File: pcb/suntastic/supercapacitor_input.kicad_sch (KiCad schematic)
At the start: 4 parts, among them J3 Supercap IN

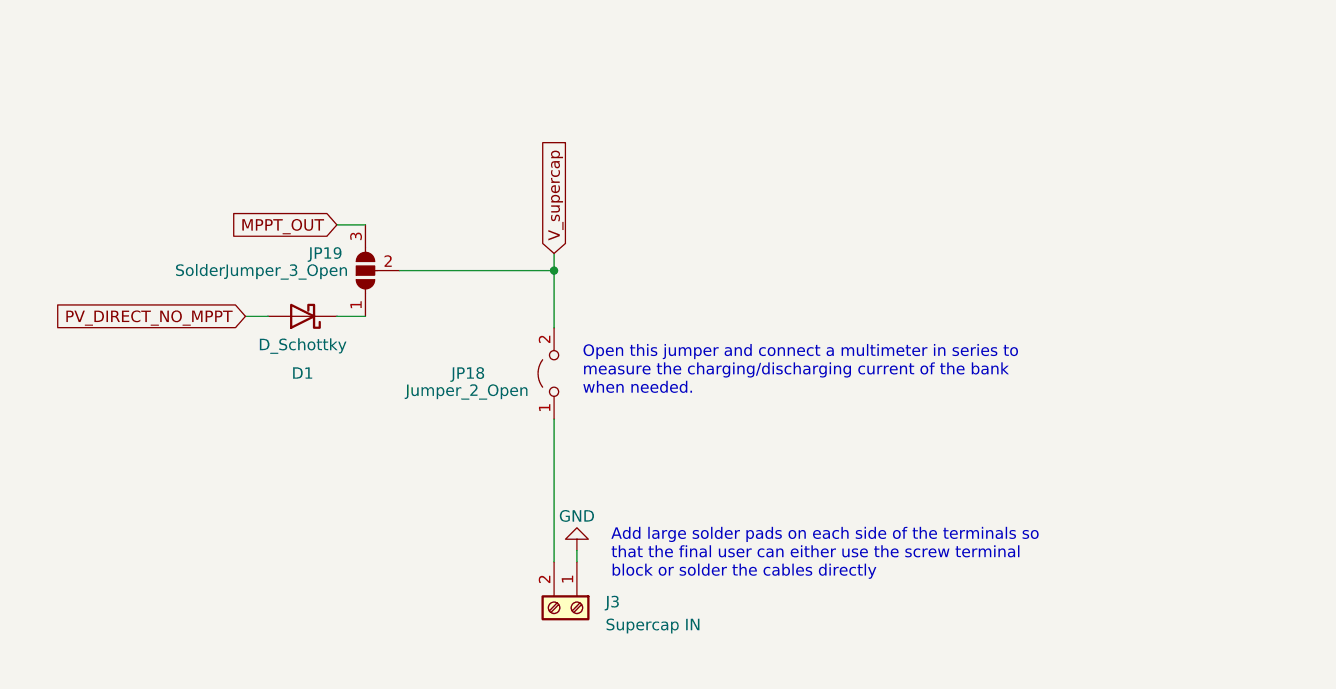
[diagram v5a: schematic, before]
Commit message: Update footprints
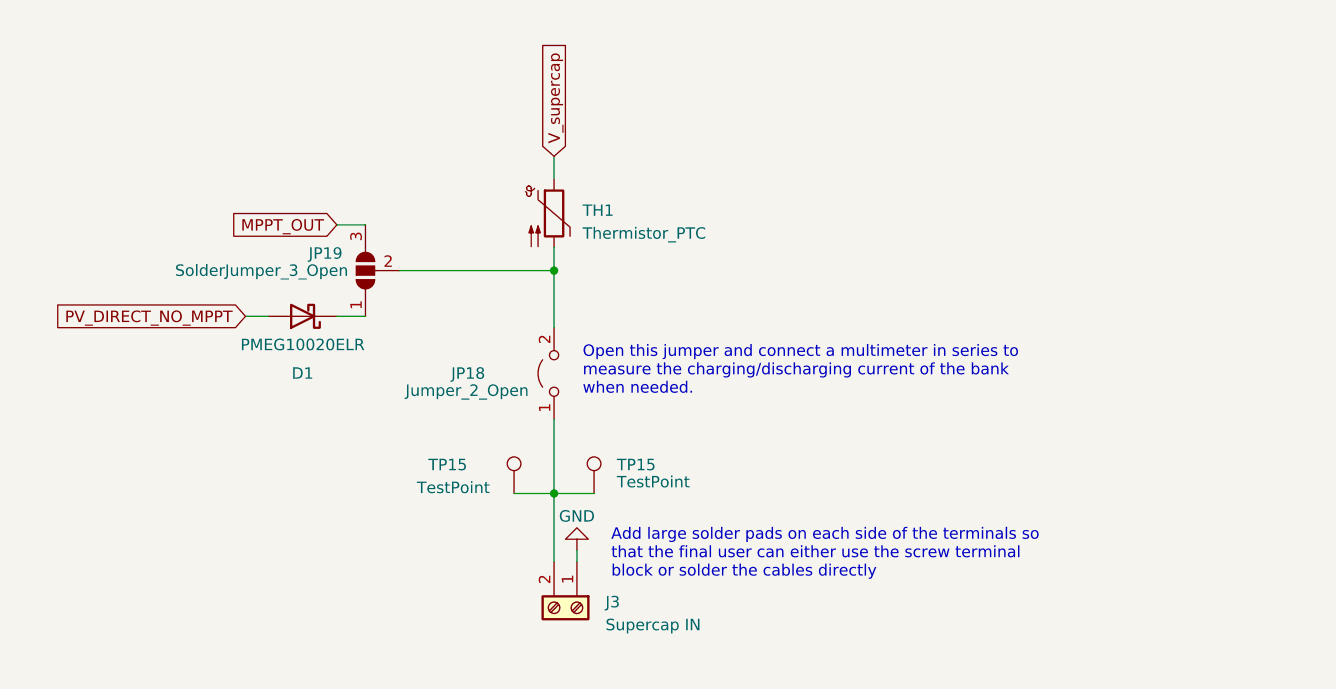
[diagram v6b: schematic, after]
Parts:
- added TH1: Thermistor_PTC, Resistor_SMD:R_0603_1608Metric_Pad0.98x0.95mm_HandSolder, symbol Device:Thermistor_PTC
- added TP15 (x2): TestPoint, TestPoint:TestPoint_THTPad_4.0x4.0mm_Drill2.0mm, symbol Connector:TestPoint
- D1: value D_Schottky -> PMEG10020ELR; footprint (none) -> Diode_SMD:D_SOD-123F
- JP19: footprint (none) -> Jumper:SolderJumper-3_P1.3mm_Open_RoundedPad1.0x1.5mm_NumberLabels
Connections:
- net V_supercap: now also TH1.1; no longer JP18.2 (B), JP19.2 (C)
- net at J3.2 (Pin_2), JP18.1 (A): now also TP15.1, TP15.1
- new net: JP18.2 (B), JP19.2 (C), TH1.2
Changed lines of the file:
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@@
     (comment 4 "The voltage tolerated by the supercapacitor bank should be AT LEAST 5.4V.")
   )
+  (junction (at 150.495 83.185) (diameter 0) (color 0 0 0 0)
+  )
   (junction (at 150.495 58.42) (diameter 0) (color 0 0 0 0)
   )
-  (wire (pts (xy 150.495 74.93) (xy 150.495 90.805))
+  (wire (pts (xy 150.495 83.185) (xy 150.495 90.805))
+    (stroke (width 0) (type default))
+  )
+  (wire (pts (xy 150.495 74.93) (xy 150.495 83.185))
     (stroke (width 0) (type default))
   )
@@
     (stroke (width 0) (type default))
   )
-  (wire (pts (xy 150.495 56.515) (xy 150.495 58.42))
-    (stroke (width 0) (type default))
-  )
   (wire (pts (xy 150.495 58.42) (xy 150.495 64.77))
     (stroke (width 0) (type default))
   )
   (wire (pts (xy 133.35 58.42) (xy 150.495 58.42))
+    (stroke (width 0) (type default))
+  )
+  (wire (pts (xy 150.495 45.72) (xy 150.495 48.26))
+    (stroke (width 0) (type default))
+  )
+  (wire (pts (xy 150.495 55.88) (xy 150.495 58.42))
+    (stroke (width 0) (type default))
+  )
+  (wire (pts (xy 146.05 83.185) (xy 150.495 83.185))
+    (stroke (width 0) (type default))
+  )
+  (wire (pts (xy 150.495 83.185) (xy 154.94 83.185))
     (stroke (width 0) (type default))
   )
@@
     )
   )
-  (global_label "V_supercap" (shape input) (at 150.495 56.515 90) (fields_autoplaced)
+  (global_label "V_supercap" (shape input) (at 150.495 45.72 90) (fields_autoplaced)
     (effects (font (size 1.27 1.27)) (justify left))
-    (property "Intersheetrefs" "${INTERSHEET_REFS}" (at 150.495 42.9655 90)
+    (property "Intersheetrefs" "${INTERSHEET_REFS}" (at 150.495 32.1705 90)
       (effects (font (size 1.27 1.27)) (justify left) hide)
     )
@@
         (path "/4d5a6178-89d6-4824-ac30-5dee40aabff2/70576ca8-d50a-4f6d-b4d0-36474c2d5281"
           (reference "JP18") (unit 1)
+        )
+      )
+    )
+  )
+  (symbol (lib_id "Connector:TestPoint") (at 154.94 83.185 0) (unit 1)
+    (in_bom yes) (on_board yes) (dnp no)
+    (property "Reference" "TP15" (at 157.48 80.01 0)
+      (effects (font (size 1.27 1.27)) (justify left))
+    )
+    (property "Value" "TestPoint" (at 157.48 81.915 0)
+      (effects (font (size 1.27 1.27)) (justify left))
+    )
+    (property "Footprint" "TestPoint:TestPoint_THTPad_4.0x4.0mm_Drill2.0mm" (at 160.02 83.185 0)
+      (effects (font (size 1.27 1.27)) hide)
+    )
+    (property "Datasheet" "~" (at 160.02 83.185 0)
+      (effects (font (size 1.27 1.27)) hide)
+    )
+    (pin "1")
+    (instances
+      (project "suntastic"
+        (path "/4d5a6178-89d6-4824-ac30-5dee40aabff2/fadcfaa3-5ba9-44dc-a564-21a258e74f25"
+          (reference "TP15") (unit 1)
+        )
+        (path "/4d5a6178-89d6-4824-ac30-5dee40aabff2/70576ca8-d50a-4f6d-b4d0-36474c2d5281"
+          (reference "TP20") (unit 1)
         )
       )
@@
       (effects (font (size 1.27 1.27)))
     )
-    (property "Value" "D_Schottky" (at 122.555 66.675 0)
+    (property "Value" "PMEG10020ELR" (at 122.555 66.675 0)
       (effects (font (size 1.27 1.27)))
     )
-    (property "Footprint" "" (at 122.555 63.5 0)
-      (effects (font (size 1.27 1.27)) hide)
-    )
-    (property "Datasheet" "~" (at 122.555 63.5 0)
+    (property "Footprint" "Diode_SMD:D_SOD-123F" (at 122.555 63.5 0)
+      (effects (font (size 1.27 1.27)) hide)
+    )
+    (property "Datasheet" "https://assets.nexperia.com/documents/data-sheet/PMEG10020ELR.pdf" (at 122.555 63.5 0)
       (effects (font (size 1.27 1.27)) hide)
     )
@@
     )
   )
+  (symbol (lib_id "Device:Thermistor_PTC") (at 150.495 52.07 0) (unit 1)
+    (in_bom yes) (on_board yes) (dnp no) (fields_autoplaced)
+    (property "Reference" "TH1" (at 153.67 51.7525 0)
+      (effects (font (size 1.27 1.27)) (justify left))
+    )
+    (property "Value" "Thermistor_PTC" (at 153.67 54.2925 0)
+      (effects (font (size 1.27 1.27)) (justify left))
+    )
+    (property "Footprint" "Resistor_SMD:R_0603_1608Metric_Pad0.98x0.95mm_HandSolder" (at 151.765 57.15 0)
+      (effects (font (size 1.27 1.27)) (justify left) hide)
+    )
+    (property "Datasheet" "~" (at 150.495 52.07 0)
+      (effects (font (size 1.27 1.27)) hide)
+    )
+    (pin "1")
+    (pin "2")
+    (instances
+      (project "suntastic"
+        (path "/4d5a6178-89d6-4824-ac30-5dee40aabff2/70576ca8-d50a-4f6d-b4d0-36474c2d5281"
+          (reference "TH1") (unit 1)
+        )
+      )
+    )
+  )
+  (symbol (lib_id "Connector:TestPoint") (at 146.05 83.185 0) (unit 1)
+    (in_bom yes) (on_board yes) (dnp no)
+    (property "Reference" "TP15" (at 136.525 80.01 0)
+      (effects (font (size 1.27 1.27)) (justify left))
+    )
+    (property "Value" "TestPoint" (at 135.255 82.55 0)
+      (effects (font (size 1.27 1.27)) (justify left))
+    )
+    (property "Footprint" "TestPoint:TestPoint_THTPad_4.0x4.0mm_Drill2.0mm" (at 151.13 83.185 0)
+      (effects (font (size 1.27 1.27)) hide)
+    )
+    (property "Datasheet" "~" (at 151.13 83.185 0)
+      (effects (font (size 1.27 1.27)) hide)
+    )
+    (pin "1")
+    (instances
+      (project "suntastic"
+        (path "/4d5a6178-89d6-4824-ac30-5dee40aabff2/fadcfaa3-5ba9-44dc-a564-21a258e74f25"
+          (reference "TP15") (unit 1)
+        )
+        (path "/4d5a6178-89d6-4824-ac30-5dee40aabff2/70576ca8-d50a-4f6d-b4d0-36474c2d5281"
+          (reference "TP19") (unit 1)
+        )
+      )
+    )
+  )
   (symbol (lib_id "Jumper:SolderJumper_3_Open") (at 129.54 58.42 90) (unit 1)
     (in_bom yes) (on_board yes) (dnp no)
@@
       (effects (font (size 1.27 1.27)) (justify left))
     )
-    (property "Footprint" "" (at 129.54 58.42 0)
-      (effects (font (size 1.27 1.27)) hide)
-    )
+    (property "Footprint" "Jumper:SolderJumper-3_P1.3mm_Open_RoundedPad1.0x1.5mm_NumberLabels" (at 129.54 58.42 0)
+      (effects (font (size 1.27 1.27)) hide)
+    )

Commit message: Update more footprints and start with PCB
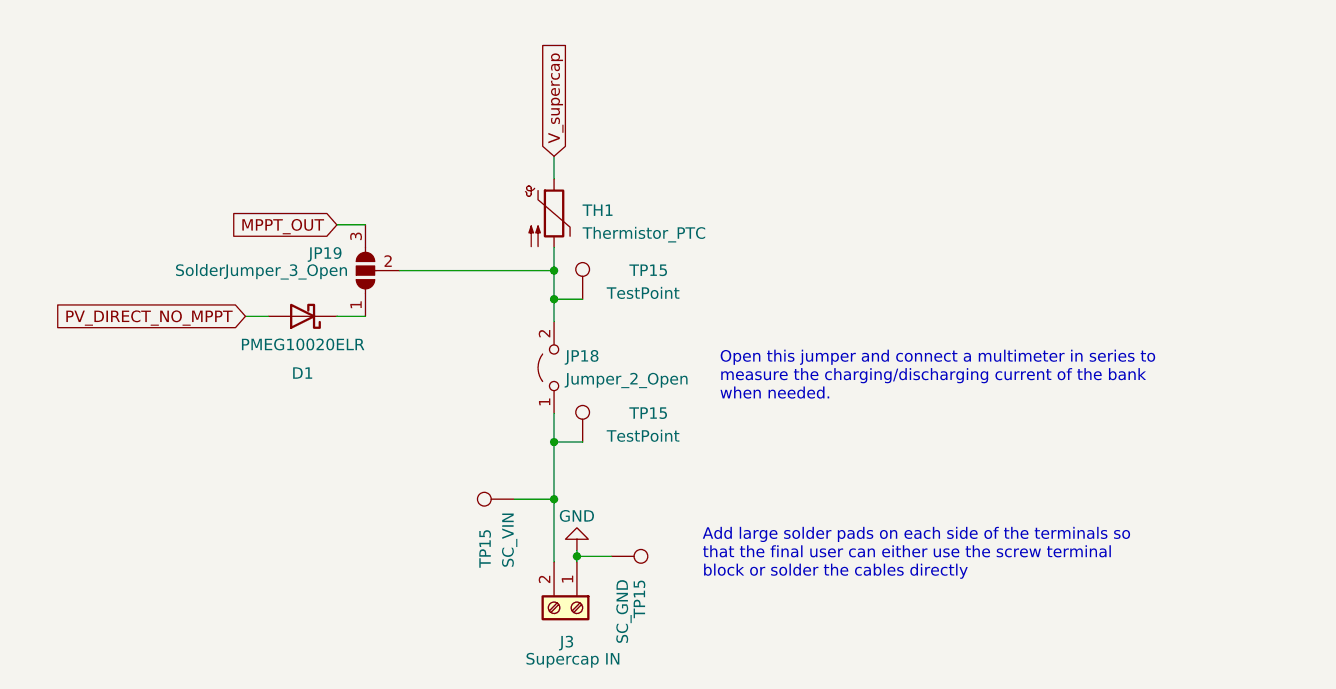
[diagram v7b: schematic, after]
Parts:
- added TP15 (x2): TestPoint, TestPoint:TestPoint_Bridge_Pitch5.08mm_Drill1.3mm, symbol Connector:TestPoint
- JP18: footprint (none) -> Jumper:SolderJumper-2_P1.3mm_Open_RoundedPad1.0x1.5mm
- TP15: value TestPoint -> SC_GND
- TP15: value TestPoint -> SC_VIN
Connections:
- net GND: now also TP15.1
- net at J3.2 (Pin_2), JP18.1 (A), TP15.1: now also TP15.1; no longer TP15.1
- net at JP18.2 (B), JP19.2 (C), TH1.2: now also TP15.1
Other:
- moved on the sheet: JP18, TP15
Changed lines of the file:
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@@
     (comment 4 "The voltage tolerated by the supercapacitor bank should be AT LEAST 5.4V.")
   )
-  (junction (at 150.495 83.185) (diameter 0) (color 0 0 0 0)
+  (junction (at 150.495 77.47) (diameter 0) (color 0 0 0 0)
   )
   (junction (at 150.495 58.42) (diameter 0) (color 0 0 0 0)
   )
-  (wire (pts (xy 150.495 83.185) (xy 150.495 90.805))
-    (stroke (width 0) (type default))
-  )
-  (wire (pts (xy 150.495 74.93) (xy 150.495 83.185))
+  (junction (at 150.495 61.595) (diameter 0) (color 0 0 0 0)
+  )
+  (junction (at 153.035 90.17) (diameter 0) (color 0 0 0 0)
+  )
+  (junction (at 150.495 83.82) (diameter 0) (color 0 0 0 0)
+  )
+  (wire (pts (xy 150.495 77.47) (xy 150.495 83.82))
     (stroke (width 0) (type default))
   )
@@
     (stroke (width 0) (type default))
   )
-  (wire (pts (xy 150.495 58.42) (xy 150.495 64.77))
+  (wire (pts (xy 153.67 77.47) (xy 150.495 77.47))
+    (stroke (width 0) (type default))
+  )
+  (wire (pts (xy 150.495 58.42) (xy 150.495 61.595))
+    (stroke (width 0) (type default))
+  )
+  (wire (pts (xy 150.495 45.72) (xy 150.495 48.26))
+    (stroke (width 0) (type default))
+  )
+  (wire (pts (xy 150.495 55.88) (xy 150.495 58.42))
+    (stroke (width 0) (type default))
+  )
+  (wire (pts (xy 153.035 90.17) (xy 156.845 90.17))
+    (stroke (width 0) (type default))
+  )
+  (wire (pts (xy 126.365 63.5) (xy 129.54 63.5))
+    (stroke (width 0) (type default))
+  )
+  (wire (pts (xy 153.035 89.535) (xy 153.035 90.17))
+    (stroke (width 0) (type default))
+  )
+  (wire (pts (xy 126.365 53.34) (xy 129.54 53.34))
+    (stroke (width 0) (type default))
+  )
+  (wire (pts (xy 153.035 90.17) (xy 153.035 90.805))
+    (stroke (width 0) (type default))
+  )
+  (wire (pts (xy 150.495 61.595) (xy 150.495 64.135))
     (stroke (width 0) (type default))
   )
@@
     (stroke (width 0) (type default))
   )
-  (wire (pts (xy 150.495 45.72) (xy 150.495 48.26))
-    (stroke (width 0) (type default))
-  )
-  (wire (pts (xy 150.495 55.88) (xy 150.495 58.42))
-    (stroke (width 0) (type default))
-  )
-  (wire (pts (xy 146.05 83.185) (xy 150.495 83.185))
-    (stroke (width 0) (type default))
-  )
-  (wire (pts (xy 150.495 83.185) (xy 154.94 83.185))
-    (stroke (width 0) (type default))
-  )
-  (wire (pts (xy 126.365 63.5) (xy 129.54 63.5))
-    (stroke (width 0) (type default))
-  )
-  (wire (pts (xy 153.035 89.535) (xy 153.035 90.805))
-    (stroke (width 0) (type default))
-  )
-  (wire (pts (xy 126.365 53.34) (xy 129.54 53.34))
+  (wire (pts (xy 150.495 83.82) (xy 150.495 90.805))
+    (stroke (width 0) (type default))
+  )
+  (wire (pts (xy 150.495 61.595) (xy 153.67 61.595))
+    (stroke (width 0) (type default))
+  )
+  (wire (pts (xy 150.495 74.295) (xy 150.495 77.47))
+    (stroke (width 0) (type default))
+  )
+  (wire (pts (xy 146.05 83.82) (xy 150.495 83.82))
     (stroke (width 0) (type default))
   )
   (text "Open this jumper and connect a multimeter in series to\nmeasure the charging/discharging current of the bank\nwhen needed."
-    (at 153.67 72.39 0)
+    (at 168.91 73.025 0)
     (effects (font (size 1.27 1.27)) (justify left bottom))
   )
   (text "Add large solder pads on each side of the terminals so\nthat the final user can either use the screw terminal \nblock or solder the cables directly"
-    (at 156.845 92.71 0)
+    (at 167.005 92.71 0)
     (effects (font (size 1.27 1.27)) (justify left bottom))
   )
@@
     )
   )
-  (symbol (lib_id "Jumper:Jumper_2_Open") (at 150.495 69.85 90) (unit 1)
-    (in_bom yes) (on_board yes) (dnp no)
-    (property "Reference" "JP18" (at 139.065 69.85 90)
+  (symbol (lib_id "Jumper:Jumper_2_Open") (at 150.495 69.215 90) (unit 1)
+    (in_bom yes) (on_board yes) (dnp no)
+    (property "Reference" "JP18" (at 151.765 67.945 90)
       (effects (font (size 1.27 1.27)) (justify right))
     )
-    (property "Value" "Jumper_2_Open" (at 133.985 71.755 90)
+    (property "Value" "Jumper_2_Open" (at 151.765 70.485 90)
       (effects (font (size 1.27 1.27)) (justify right))
     )
-    (property "Footprint" "" (at 150.495 69.85 0)
-      (effects (font (size 1.27 1.27)) hide)
-    )
-    (property "Datasheet" "~" (at 150.495 69.85 0)
+    (property "Footprint" "Jumper:SolderJumper-2_P1.3mm_Open_RoundedPad1.0x1.5mm" (at 150.495 69.215 0)
+      (effects (font (size 1.27 1.27)) hide)
+    )
+    (property "Datasheet" "~" (at 150.495 69.215 0)
       (effects (font (size 1.27 1.27)) hide)
     )
@@
     )
   )
-  (symbol (lib_id "Connector:TestPoint") (at 154.94 83.185 0) (unit 1)
-    (in_bom yes) (on_board yes) (dnp no)
-    (property "Reference" "TP15" (at 157.48 80.01 0)
-      (effects (font (size 1.27 1.27)) (justify left))
-    )
-    (property "Value" "TestPoint" (at 157.48 81.915 0)
-      (effects (font (size 1.27 1.27)) (justify left))
-    )
-    (property "Footprint" "TestPoint:TestPoint_THTPad_4.0x4.0mm_Drill2.0mm" (at 160.02 83.185 0)
-      (effects (font (size 1.27 1.27)) hide)
-    )
-    (property "Datasheet" "~" (at 160.02 83.185 0)
+  (symbol (lib_id "Connector:TestPoint") (at 153.67 61.595 0) (mirror y) (unit 1)
+    (in_bom yes) (on_board yes) (dnp no)
+    (property "Reference" "TP15" (at 163.195 58.42 0)
+      (effects (font (size 1.27 1.27)) (justify left))
+    )
+    (property "Value" "TestPoint" (at 164.465 60.96 0)
+      (effects (font (size 1.27 1.27)) (justify left))
+    )
+    (property "Footprint" "TestPoint:TestPoint_Bridge_Pitch5.08mm_Drill1.3mm" (at 148.59 61.595 0)
+      (effects (font (size 1.27 1.27)) hide)
+    )
+    (property "Datasheet" "~" (at 148.59 61.595 0)
+      (effects (font (size 1.27 1.27)) hide)
+    )
+    (pin "1")
+    (instances
+      (project "suntastic"
+        (path "/4d5a6178-89d6-4824-ac30-5dee40aabff2/fadcfaa3-5ba9-44dc-a564-21a258e74f25"
+          (reference "TP15") (unit 1)
+        )
+        (path "/4d5a6178-89d6-4824-ac30-5dee40aabff2/70576ca8-d50a-4f6d-b4d0-36474c2d5281"
+          (reference "TP21") (unit 1)
+        )
+      )
+    )
+  )
+  (symbol (lib_id "Connector:TestPoint") (at 153.67 77.47 0) (mirror y) (unit 1)
+    (in_bom yes) (on_board yes) (dnp no)
+    (property "Reference" "TP15" (at 163.195 74.295 0)
+      (effects (font (size 1.27 1.27)) (justify left))
+    )
+    (property "Value" "TestPoint" (at 164.465 76.835 0)
+      (effects (font (size 1.27 1.27)) (justify left))
+    )
+    (property "Footprint" "TestPoint:TestPoint_Bridge_Pitch5.08mm_Drill1.3mm" (at 148.59 77.47 0)
+      (effects (font (size 1.27 1.27)) hide)
+    )
+    (property "Datasheet" "~" (at 148.59 77.47 0)
+      (effects (font (size 1.27 1.27)) hide)
+    )
+    (pin "1")
+    (instances
+      (project "suntastic"
+        (path "/4d5a6178-89d6-4824-ac30-5dee40aabff2/fadcfaa3-5ba9-44dc-a564-21a258e74f25"
+          (reference "TP15") (unit 1)
+        )
+        (path "/4d5a6178-89d6-4824-ac30-5dee40aabff2/70576ca8-d50a-4f6d-b4d0-36474c2d5281"
+          (reference "TP22") (unit 1)
+        )
+      )
+    )
+  )
+  (symbol (lib_id "Connector:TestPoint") (at 156.845 90.17 270) (unit 1)
+    (in_bom yes) (on_board yes) (dnp no)
+    (property "Reference" "TP15" (at 160.02 92.71 0)
+      (effects (font (size 1.27 1.27)) (justify left))
+    )
+    (property "Value" "SC_GND" (at 158.115 92.71 0)
+      (effects (font (size 1.27 1.27)) (justify left))
+    )
+    (property "Footprint" "TestPoint:TestPoint_THTPad_4.0x4.0mm_Drill2.0mm" (at 156.845 95.25 0)
+      (effects (font (size 1.27 1.27)) hide)
+    )
+    (property "Datasheet" "~" (at 156.845 95.25 0)
       (effects (font (size 1.27 1.27)) hide)
     )
@@
   )
   (symbol (lib_id "Connector:Screw_Terminal_01x02") (at 153.035 95.885 270) (unit 1)
-    (in_bom yes) (on_board yes) (dnp no) (fields_autoplaced)
-    (property "Reference" "J3" (at 156.21 95.25 90)
-      (effects (font (size 1.27 1.27)) (justify left))
-    )
-    (property "Value" "Supercap IN" (at 156.21 97.79 90)
+    (in_bom yes) (on_board yes) (dnp no)
+    (property "Reference" "J3" (at 151.13 99.695 90)
+      (effects (font (size 1.27 1.27)) (justify left))
+    )
+    (property "Value" "Supercap IN" (at 147.32 101.6 90)
       (effects (font (size 1.27 1.27)) (justify left))
     )
@@
     )
   )
-  (symbol (lib_id "Connector:TestPoint") (at 146.05 83.185 0) (unit 1)
-    (in_bom yes) (on_board yes) (dnp no)
-    (property "Reference" "TP15" (at 136.525 80.01 0)
-      (effects (font (size 1.27 1.27)) (justify left))
-    )
-    (property "Value" "TestPoint" (at 135.255 82.55 0)
-      (effects (font (size 1.27 1.27)) (justify left))
-    )
-    (property "Footprint" "TestPoint:TestPoint_THTPad_4.0x4.0mm_Drill2.0mm" (at 151.13 83.185 0)
-      (effects (font (size 1.27 1.27)) hide)
-    )
-    (property "Datasheet" "~" (at 151.13 83.185 0)
-      (effects (font (size 1.27 1.27)) hide)
-    )
+  (symbol (lib_id "Connector:TestPoint") (at 146.05 83.82 90) (unit 1)
+    (in_bom yes) (on_board yes) (dnp no)
+    (property "Reference" "TP15" (at 142.875 91.44 0)
+      (effects (font (size 1.27 1.27)) (justify left))
+    )
+    (property "Value" "SC_VIN" (at 145.415 91.44 0)
+      (effects (font (size 1.27 1.27)) (justify left))
+    )
+    (property "Footprint" "TestPoint:TestPoint_THTPad_4.0x4.0mm_Drill2.0mm" (at 146.05 78.74 0)
+      (effects (font (size 1.27 1.27)) hide)
+    )
+    (property "Datasheet" "~" (at 146.05 78.74 0)
+      (effects (font (size 1.27 1.27)) hide)
+    )
